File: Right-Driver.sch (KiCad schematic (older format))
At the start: 4 parts

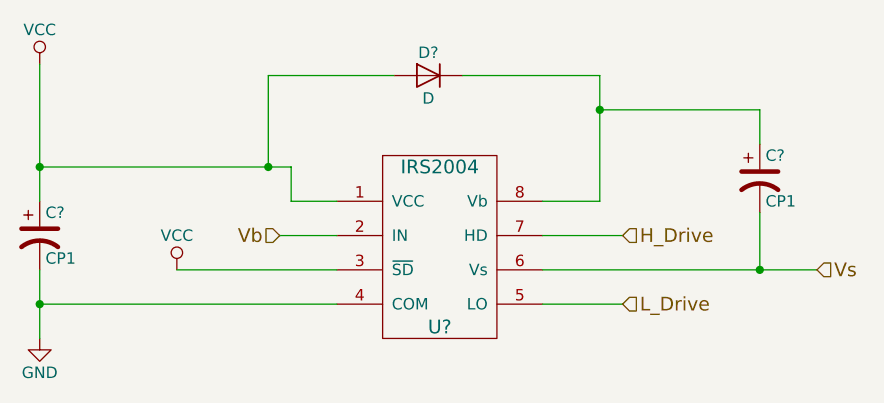
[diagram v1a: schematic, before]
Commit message: Updated the System pull-up resistors
Turns out that the IRS2004 requires a 1k pull up to work smoothly.
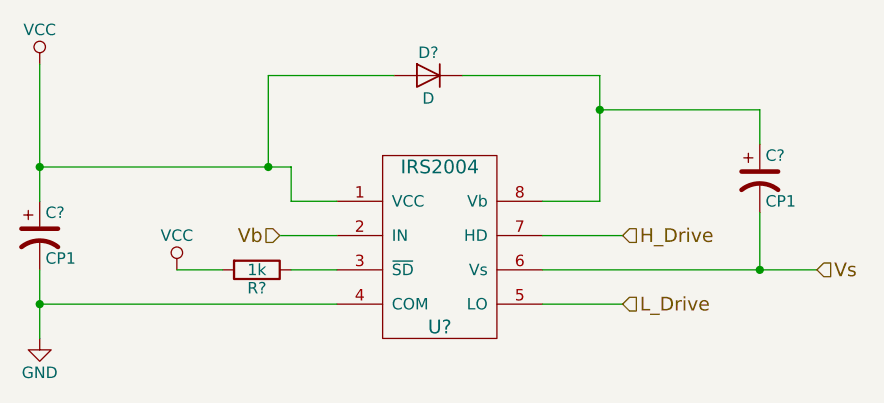
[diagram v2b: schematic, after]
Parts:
- added R?: 1k, symbol R
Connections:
- net VCC: now also R?.2; no longer U?.3 (~SD)
- new net: R?.1, U?.3 (~SD)
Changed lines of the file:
@@
 	2350 3000 2350 3300
-Wire Wire Line
-	2950 3000 3650 3000
 Wire Wire Line
 	3650 3150 2350 3150
@@
 	4550 3150 4900 3150
 Wire Wire Line
-	4550 2700 4800 2700
+	4800 2700 4550 2700
 Wire Wire Line
-	4800 2700 4800 2150
+	4800 2150 4800 2700
 Wire Wire Line
 	4800 2150 4200 2150
@@
 	5500 2750 5500 3000
 Connection ~ 5500 3000
+$Comp
+L R R?
+U 1 1 58FE3C1F
+P 3300 3000
+F 0 "R?" V 3380 3000 50  0000 C CNN
+F 1 "1k" V 3300 3000 50  0000 C CNN
+F 2 "" V 3230 3000 50  0000 C CNN
+F 3 "" H 3300 3000 50  0000 C CNN
+	1    3300 3000
+	0    1    1    0
+$EndComp
+Wire Wire Line
+	3450 3000 3650 3000
+Wire Wire Line
+	2950 3000 3150 3000
 $EndSCHEMATC
